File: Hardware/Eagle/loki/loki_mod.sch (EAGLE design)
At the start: 37 parts

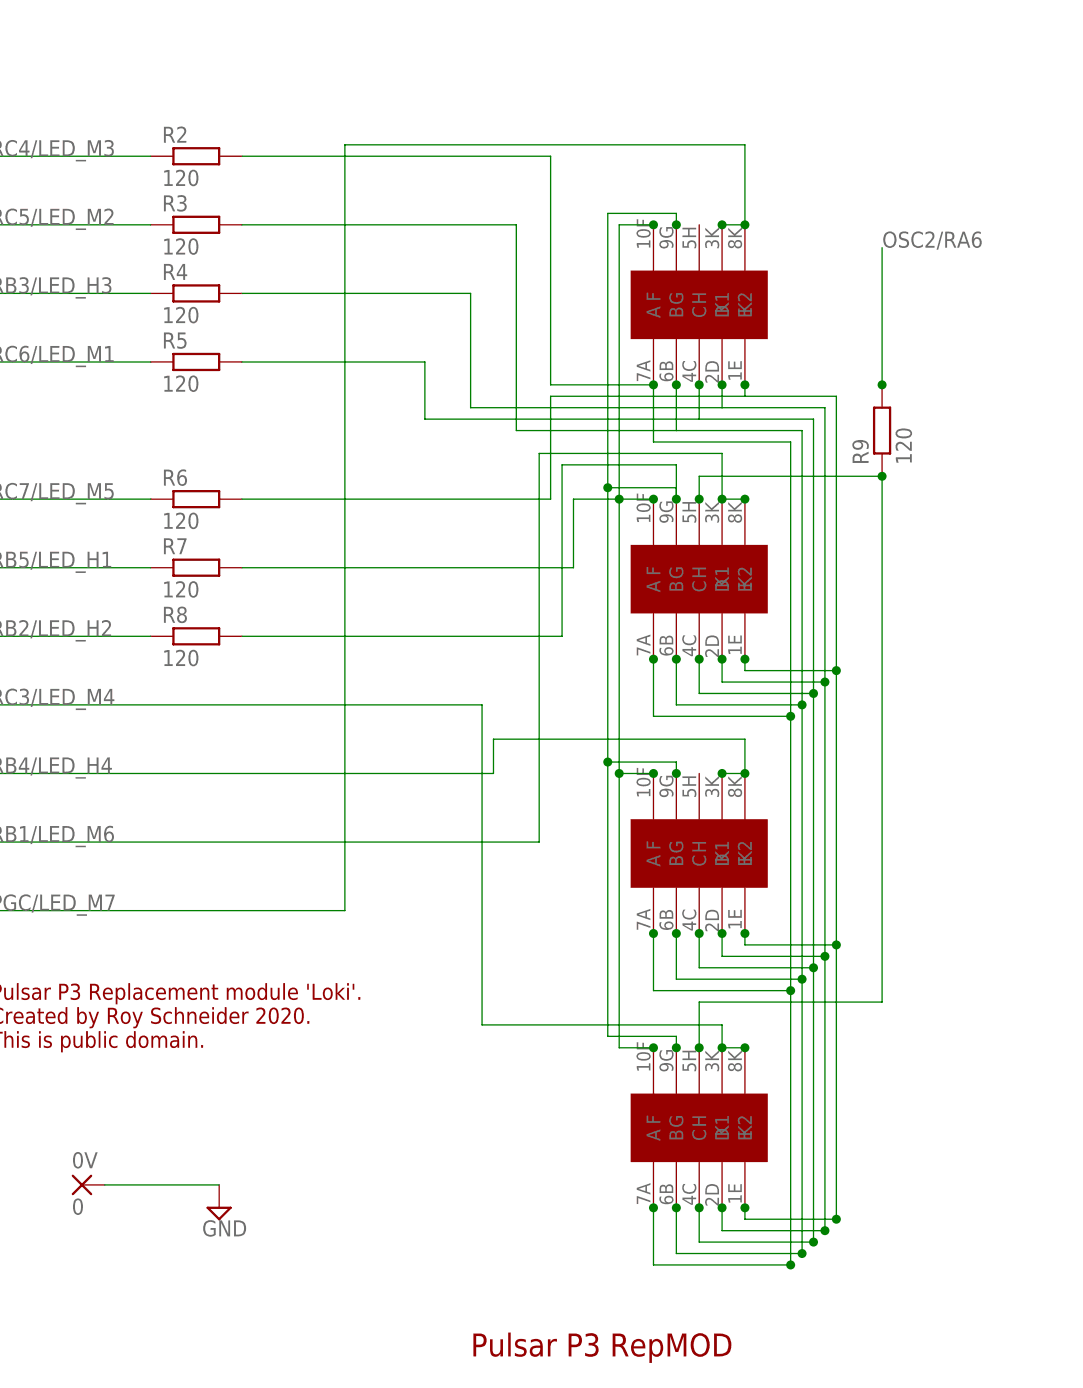
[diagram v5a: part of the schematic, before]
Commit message: Optimized layout for manual soldering.
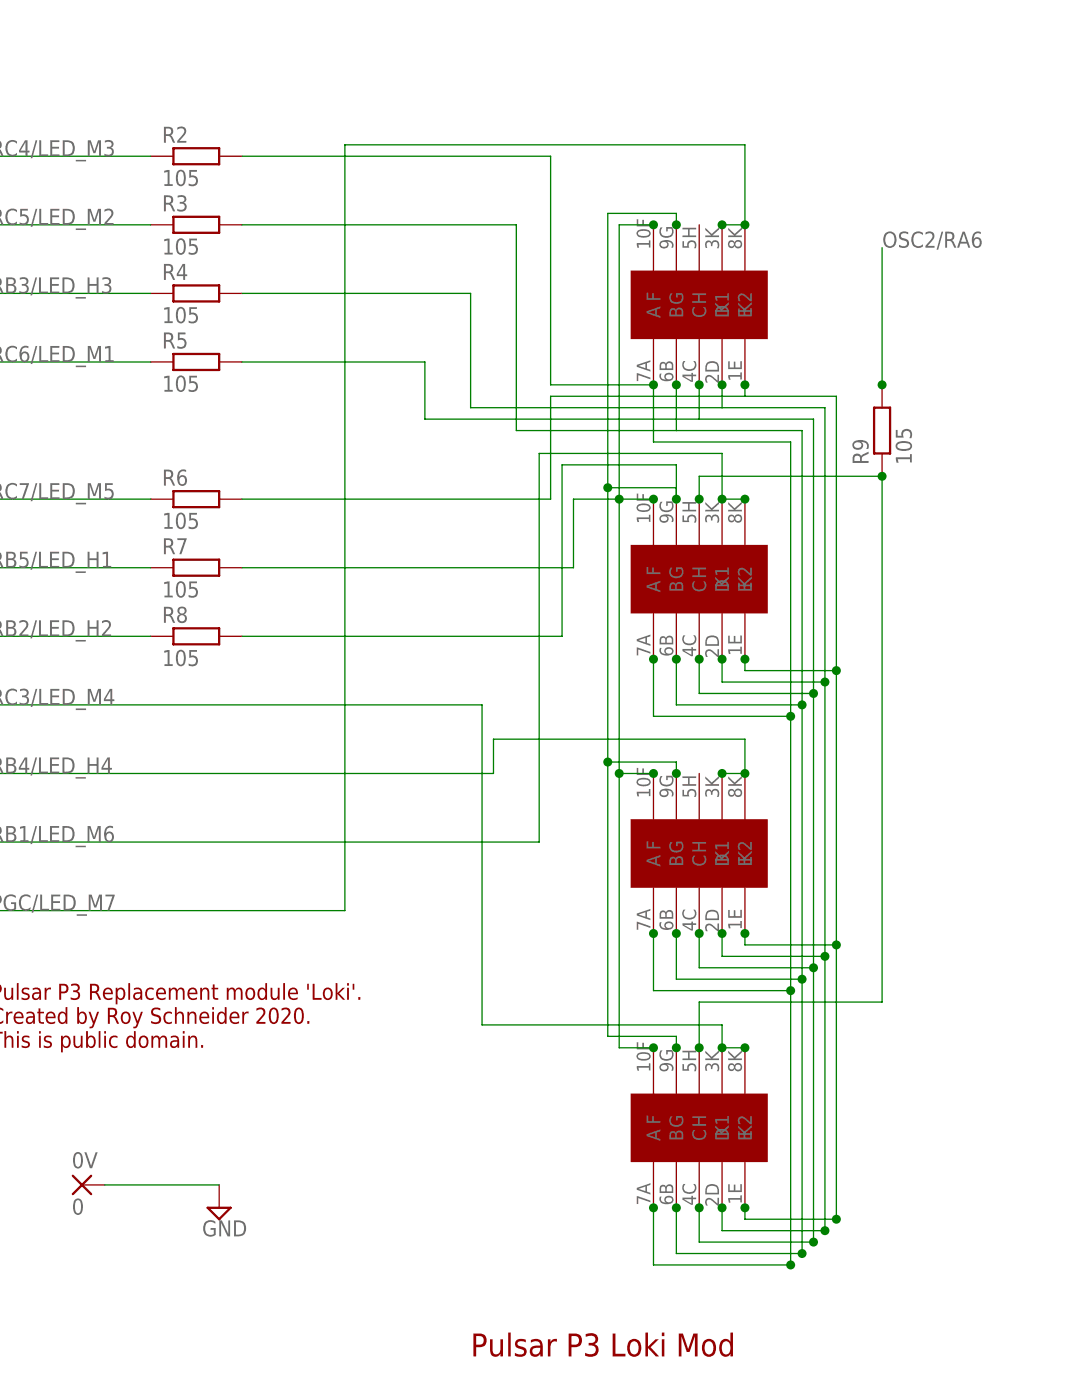
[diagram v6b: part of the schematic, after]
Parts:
- R2, R3, R4, R5, R6, R7, R8, R9: value 120 -> 105
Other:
- note added: "Pulsar P3 Loki Mod"
- note removed: "Pulsar P3 RepMOD"
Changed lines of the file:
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@@
 <part name="SUPPLY2" library="supply2" deviceset="GND" device=""/>
 <part name="SUPPLY3" library="supply2" deviceset="GND" device=""/>
-<part name="R2" library="resistor" deviceset="R-EU_" device="R0402" value="120"/>
-<part name="R3" library="resistor" deviceset="R-EU_" device="R0402" value="120"/>
-<part name="R4" library="resistor" deviceset="R-EU_" device="R0402" value="120"/>
-<part name="R5" library="resistor" deviceset="R-EU_" device="R0402" value="120"/>
-<part name="R6" library="resistor" deviceset="R-EU_" device="R0402" value="120"/>
-<part name="R7" library="resistor" deviceset="R-EU_" device="R0402" value="120"/>
-<part name="R8" library="resistor" deviceset="R-EU_" device="R0402" value="120"/>
+<part name="R2" library="resistor" deviceset="R-EU_" device="R0402" value="105"/>
+<part name="R3" library="resistor" deviceset="R-EU_" device="R0402" value="105"/>
+<part name="R4" library="resistor" deviceset="R-EU_" device="R0402" value="105"/>
+<part name="R5" library="resistor" deviceset="R-EU_" device="R0402" value="105"/>
+<part name="R6" library="resistor" deviceset="R-EU_" device="R0402" value="105"/>
+<part name="R7" library="resistor" deviceset="R-EU_" device="R0402" value="105"/>
+<part name="R8" library="resistor" deviceset="R-EU_" device="R0402" value="105"/>
 <part name="R14" library="resistor" deviceset="R-EU_" device="R0402" value="4.7k"/>
 <part name="R15" library="resistor" deviceset="R-EU_" device="R0402" value="4.7k"/>
@@
 <part name="10M" library="l104g" deviceset="L104G" device=""/>
 <part name="1M" library="l104g" deviceset="L104G" device=""/>
-<part name="R9" library="resistor" deviceset="R-EU_" device="R0402" value="120"/>
+<part name="R9" library="resistor" deviceset="R-EU_" device="R0402" value="105"/>
 </parts>
 <sheets>
@@
 Created by Roy Schneider 2020.
 This is public domain.</text>
-<text x="-22.86" y="-110.49" size="2.54" layer="94" font="vector">Pulsar P3 RepMOD</text>
+<text x="-22.86" y="-110.49" size="2.54" layer="94" font="vector">Pulsar P3 Loki Mod</text>
 </plain>
 <instances>

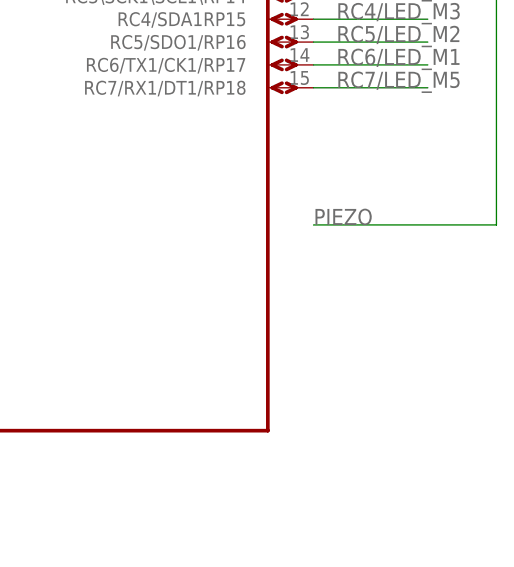
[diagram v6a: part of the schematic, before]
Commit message: Added the buzzer solder pad for the 'Loki' board.
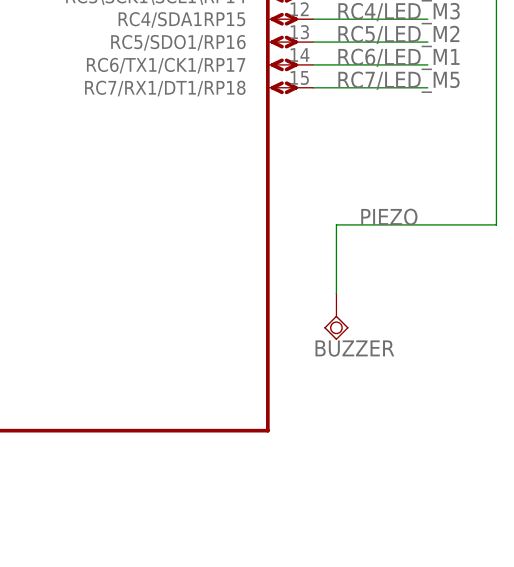
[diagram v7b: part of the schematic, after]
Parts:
- added BUZZER: TPSQTP10SQ, testpad:TPSQTP10SQ
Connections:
- net PIEZO: now also BUZZER.TP
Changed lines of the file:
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@@
 <part name="1M" library="l104g" deviceset="L104G" device=""/>
 <part name="R9" library="resistor" deviceset="R-EU_" device="R0402" value="105"/>
+<part name="BUZZER" library="testpad" deviceset="TPSQ" device="TP10SQ"/>
 </parts>
 <sheets>
@@
 <instance part="1M" gate="G$1" x="12.7" y="-63.5" rot="R90"/>
 <instance part="R9" gate="G$1" x="22.86" y="-7.62" rot="R90"/>
+<instance part="BUZZER" gate="G$1" x="30.48" y="63.5"/>
 </instances>
 <busses>
@@
 <wire x1="27.94" y1="101.6" x2="48.26" y2="101.6" width="0.1524" layer="91"/>
 <wire x1="48.26" y1="101.6" x2="48.26" y2="73.66" width="0.1524" layer="91"/>
-<wire x1="48.26" y1="73.66" x2="27.94" y2="73.66" width="0.1524" layer="91"/>
-<label x="27.94" y="73.66" size="1.778" layer="95"/>
-</segment>
-</net>
+<wire x1="48.26" y1="73.66" x2="30.48" y2="73.66" width="0.1524" layer="91"/>
+<label x="33.02" y="73.66" size="1.778" layer="95"/>
+<wire x1="30.48" y1="73.66" x2="30.48" y2="66.04" width="0.1524" layer="91"/>
+<pinref part="BUZZER" gate="G$1" pin="TP"/>
+</segment>
+</net>

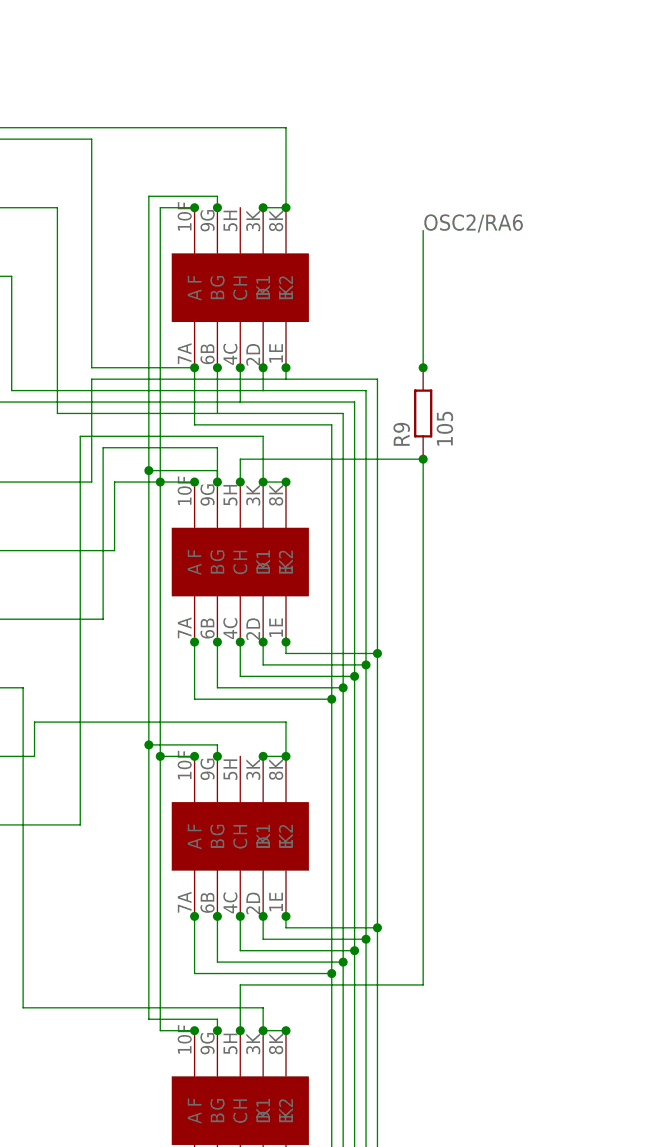
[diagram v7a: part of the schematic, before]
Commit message: Connected unused dots for digit 1 and 3.
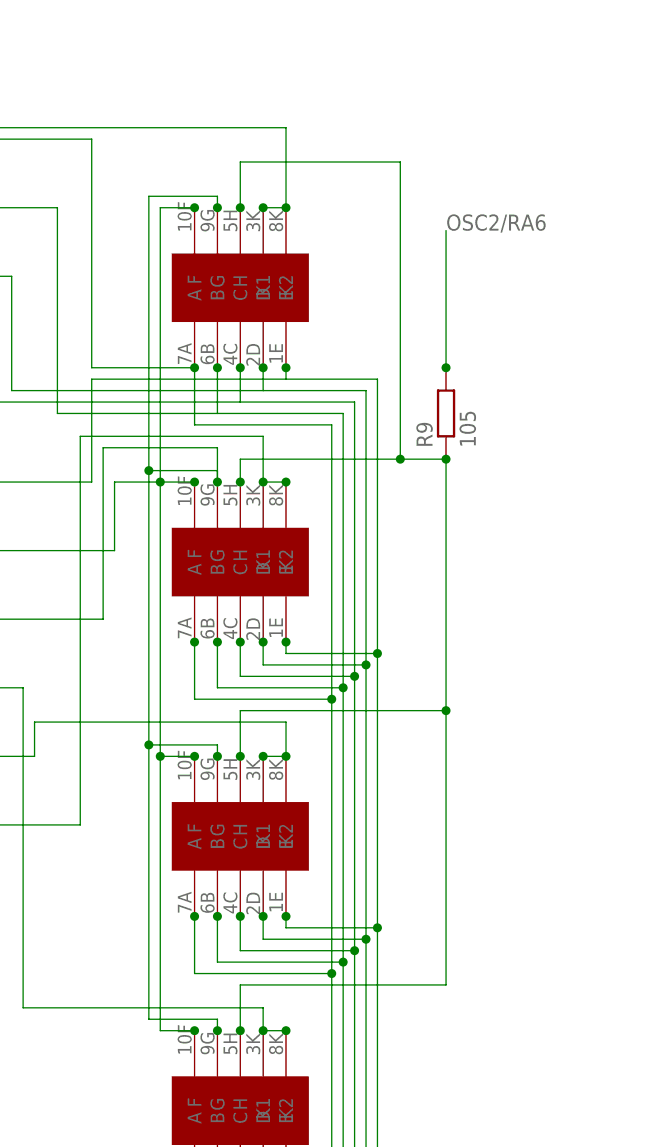
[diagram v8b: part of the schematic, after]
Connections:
- removed net N$1: 1H.H, 1M.H, R9.1
- new net N$6: 10H.H, 10M.H, 1H.H, 1M.H, R9.1
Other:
- moved on the sheet: R9
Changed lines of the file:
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@@
 <instance part="10M" gate="G$1" x="12.7" y="-33.02" rot="R90"/>
 <instance part="1M" gate="G$1" x="12.7" y="-63.5" rot="R90"/>
-<instance part="R9" gate="G$1" x="22.86" y="-7.62" rot="R90"/>
+<instance part="R9" gate="G$1" x="25.4" y="-7.62" rot="R90"/>
 <instance part="BUZZER" gate="G$1" x="30.48" y="63.5"/>
 </instances>
@@
 <segment>
 <pinref part="R9" gate="G$1" pin="2"/>
-<wire x1="22.86" y1="-2.54" x2="22.86" y2="12.7" width="0.1524" layer="91"/>
-<label x="22.86" y="12.7" size="1.778" layer="95"/>
-<junction x="22.86" y="-2.54"/>
+<wire x1="25.4" y1="-2.54" x2="25.4" y2="12.7" width="0.1524" layer="91"/>
+<label x="25.4" y="12.7" size="1.778" layer="95"/>
+<junction x="25.4" y="-2.54"/>
 </segment>
 </net>
@@
 </segment>
 </net>
-<net name="N$1" class="0">
-<segment>
-<pinref part="1H" gate="G$1" pin="H"/>
-<wire x1="2.54" y1="-15.24" x2="2.54" y2="-12.7" width="0.1524" layer="91"/>
-<wire x1="2.54" y1="-12.7" x2="22.86" y2="-12.7" width="0.1524" layer="91"/>
-<pinref part="R9" gate="G$1" pin="1"/>
-<junction x="22.86" y="-12.7"/>
-<junction x="2.54" y="-15.24"/>
-<pinref part="1M" gate="G$1" pin="H"/>
-<wire x1="2.54" y1="-76.2" x2="2.54" y2="-71.12" width="0.1524" layer="91"/>
-<wire x1="2.54" y1="-71.12" x2="22.86" y2="-71.12" width="0.1524" layer="91"/>
-<wire x1="22.86" y1="-71.12" x2="22.86" y2="-12.7" width="0.1524" layer="91"/>
-<junction x="2.54" y="-76.2"/>
-</segment>
-</net>
 <net name="PIEZO" class="0">
 <segment>
@@
 </segment>
 </net>
+<net name="N$6" class="0">
+<segment>
+<pinref part="10M" gate="G$1" pin="H"/>
+<wire x1="2.54" y1="-45.72" x2="2.54" y2="-40.64" width="0.1524" layer="91"/>
+<pinref part="1H" gate="G$1" pin="H"/>
+<wire x1="2.54" y1="-15.24" x2="2.54" y2="-12.7" width="0.1524" layer="91"/>
+<wire x1="2.54" y1="-12.7" x2="20.32" y2="-12.7" width="0.1524" layer="91"/>
+<pinref part="R9" gate="G$1" pin="1"/>
+<junction x="25.4" y="-12.7"/>
+<junction x="2.54" y="-15.24"/>
+<pinref part="1M" gate="G$1" pin="H"/>
+<wire x1="2.54" y1="-76.2" x2="2.54" y2="-71.12" width="0.1524" layer="91"/>
+<wire x1="2.54" y1="-71.12" x2="25.4" y2="-71.12" width="0.1524" layer="91"/>
+<wire x1="25.4" y1="-71.12" x2="25.4" y2="-40.64" width="0.1524" layer="91"/>
+<junction x="2.54" y="-76.2"/>
+<pinref part="10H" gate="G$1" pin="H"/>
+<wire x1="25.4" y1="-40.64" x2="25.4" y2="-12.7" width="0.1524" layer="91"/>
+<wire x1="2.54" y1="15.24" x2="2.54" y2="20.32" width="0.1524" layer="91"/>
+<wire x1="2.54" y1="20.32" x2="20.32" y2="20.32" width="0.1524" layer="91"/>
+<wire x1="20.32" y1="20.32" x2="20.32" y2="-12.7" width="0.1524" layer="91"/>
+<wire x1="20.32" y1="-12.7" x2="25.4" y2="-12.7" width="0.1524" layer="91"/>
+<junction x="2.54" y="15.24"/>
+<junction x="25.4" y="-40.64"/>
+<wire x1="2.54" y1="-40.64" x2="25.4" y2="-40.64" width="0.1524" layer="91"/>
+<junction x="2.54" y="-45.72"/>
+<junction x="20.32" y="-12.7"/>
+</segment>
+</net>
